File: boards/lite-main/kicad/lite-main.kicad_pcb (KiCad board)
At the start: 2 copper layers, 100 x 90 mm, 149 parts, among them J1 TYPE-C-31-M-12, J2 RCA line in, J3 RCA sub out, J4 DB128V-5.08-4P, Q1 AO4485, Q2 MMBT3904, Q3 MMBT3904, Q4 MMBT3904, SW1 TS-1187A, SW2 TS-1187A, SW3 TS-1187A, U1 CH224A, U2 TPS54302, U3 SY8089A1AAC, U4 LP5907-3.3, U5 ESP32-WROVER-E-N8R8, U6 CH340B, U7 ES8388, U8 TPA3118D2, U9 IRM-3638T

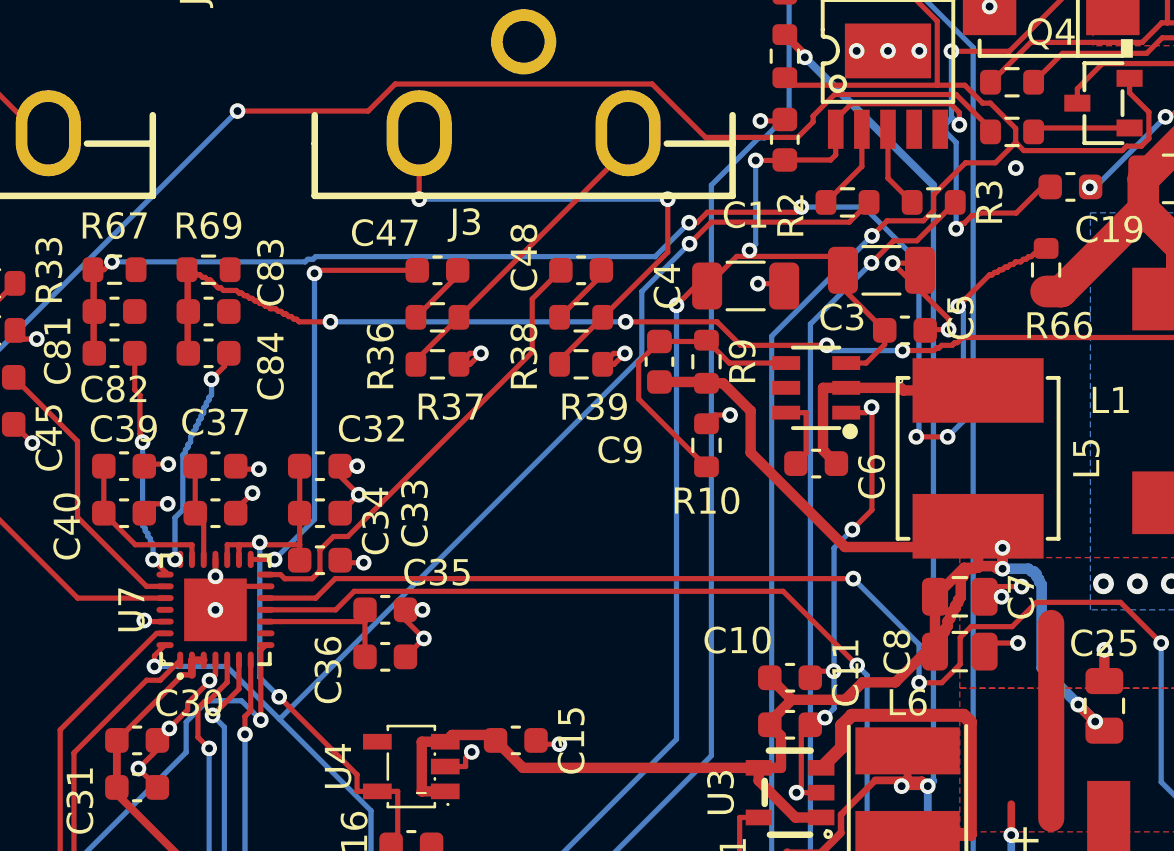
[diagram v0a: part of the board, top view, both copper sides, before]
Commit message: Lite's sub outs mute on power loss (review-3 R3-AUDIO-2): a +5V sense holds two back-to-back 2N7002s off; when +5V drops they short SUB_L/SUB_R to GND from a 22 uF reservoir for seconds
The as-built thump at a 10k sub input was -1.61 V (full scale); with the mute
it is -25 mV (docs/review-3/sims/fix/lite_mute/tb_powerloss). Off, the gates
sit at Q12's saturation, so the sub line has to stay above -Vth(min) 1.0 V:
firmware caps LOUT2/ROUT2 at -6 dB (0.71 V peak, tb_play_cap; was +4.5 dB).
Q11 is an MMBT3904 as a diode, so no new part numbers beyond the basic
2N7002 (C8545). 9 parts placed in the free pocket under R37-R39 and routed
with miniroute; two GND vias rejoin the pour the new tracks split. DRC clean
(zones refilled), drc_routed and dfm gates pass, fab files regenerated.

Also Lite's thermal governor 13 -> 9 W a channel (R3-LAYOUT-13).
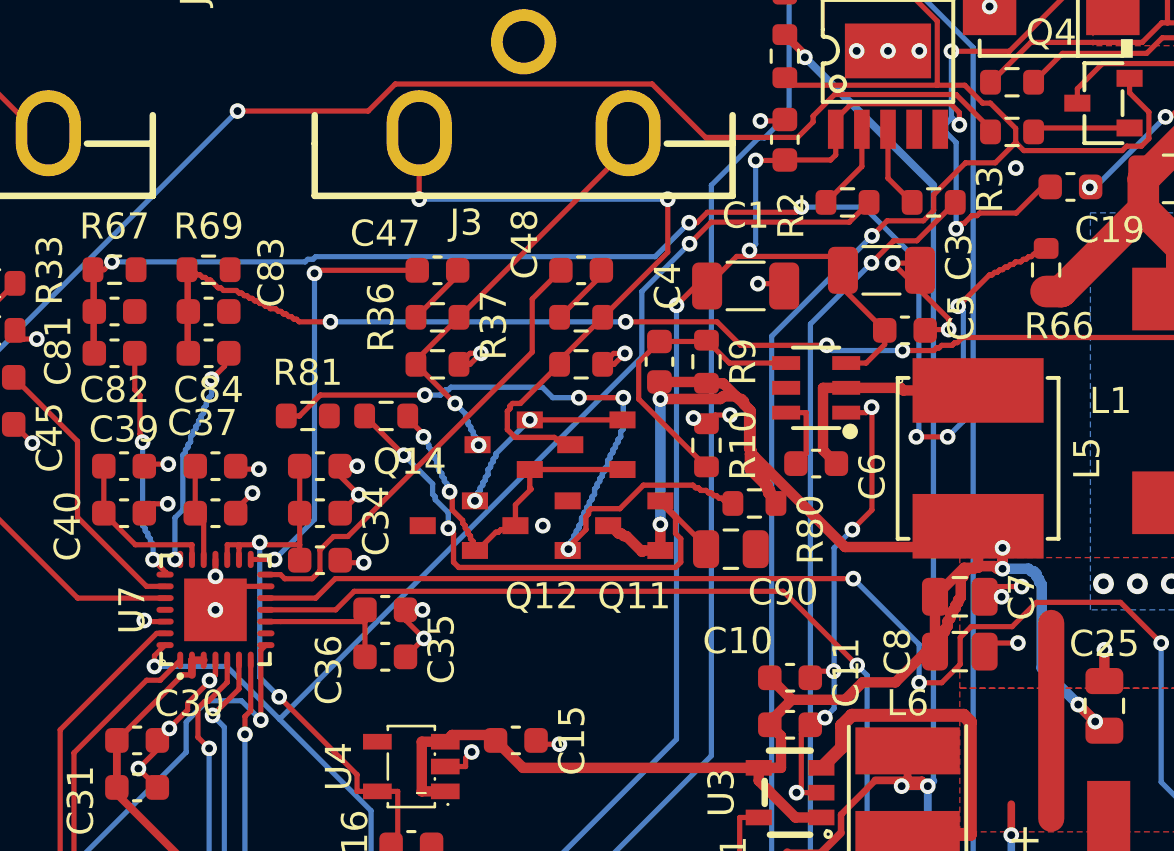
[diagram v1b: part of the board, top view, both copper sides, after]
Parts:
- added C90: 22uF, Capacitor_SMD:C_0805_2012Metric, F.Cu at (72.6, 93.0)
- added Q11: MMBT3904, aiee:SOT-23-3_L2.9-W1.3-P1.90-LS2.4-BR, F.Cu at (68.9, 92.1)
- added Q12: MMBT3904, aiee:SOT-23-3_L2.9-W1.3-P1.90-LS2.4-BR, F.Cu at (65.3, 92.1)
- added Q13: 2N7002, aiee:SOT-23-3_L2.9-W1.3-P1.90-LS2.4-BR, F.Cu at (63.9, 89.0)
- added Q14: 2N7002, aiee:SOT-23-3_L2.9-W1.3-P1.90-LS2.4-BR, F.Cu at (61.8, 92.1)
- added Q15: 2N7002, aiee:SOT-23-3_L2.9-W1.3-P1.90-LS2.4-BR, F.Cu at (67.5, 89.0)
- added R80: 120k, Resistor_SMD:R_0603_1608Metric, F.Cu at (73.5, 91.2)
- added R81: 22k, Resistor_SMD:R_0603_1608Metric, F.Cu at (56.4, 87.9)
- added R82: 47k, Resistor_SMD:R_0603_1608Metric, F.Cu at (59.4, 87.9)
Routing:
- net /MUTE_DET: track 0.00 -> 28.2 mm, vias 0 -> 4
- net /MUTE_RES: track 0.00 -> 21.1 mm, vias 0 -> 2
- net +5V: track 68.9 -> 87.2 mm, vias 4 -> 6
- net /SUB_MUTE: track 0.00 -> 14.2 mm, vias 0 -> 2
- net /MUTE_S: track 0.00 -> 7.52 mm, vias 0 -> 2
- net /SUB_R: track 21.1 -> 27.3 mm
- net /SUB_L: track 11.8 -> 15.9 mm, vias 0 -> 2
- net GND: vias 117 -> 119

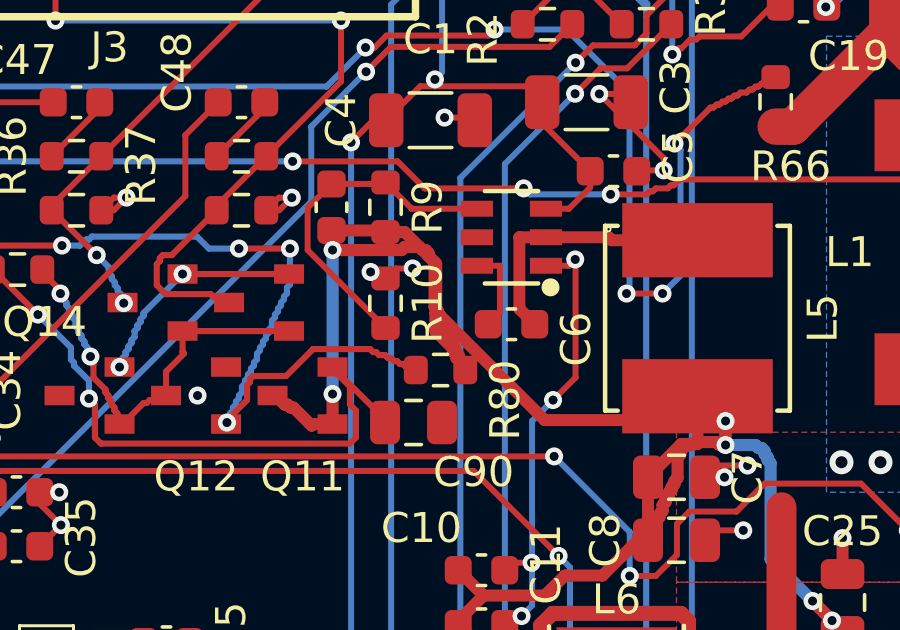
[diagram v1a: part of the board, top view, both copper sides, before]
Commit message: Lite sub build-out R36/R38 100R -> 1k (R4-PAD-1), fab regenerated
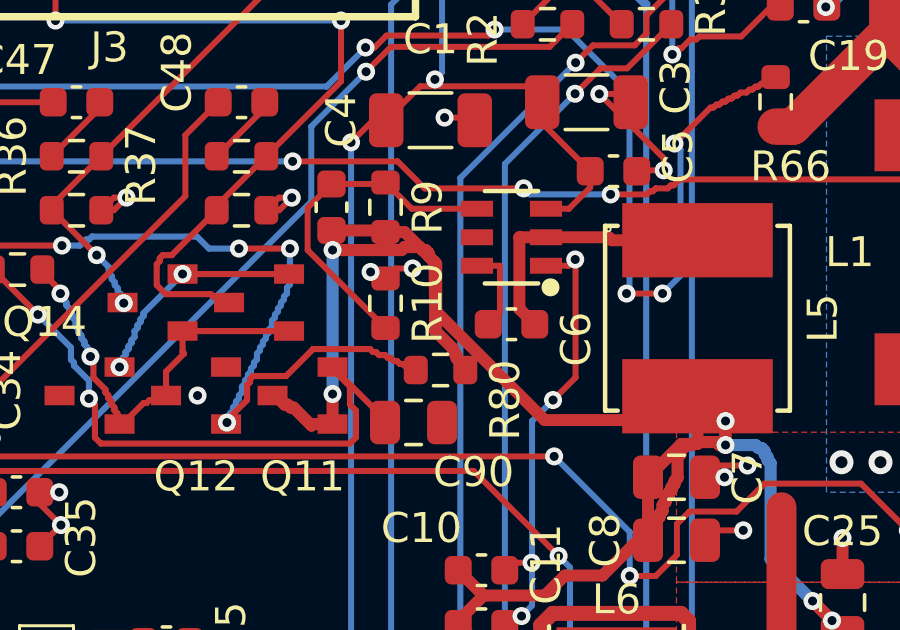
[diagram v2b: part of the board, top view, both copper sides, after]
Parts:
- R36, R38: value 100R -> 1k
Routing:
- net +5V: track 87.2 -> 85.5 mm
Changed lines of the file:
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@@
 			)
 		)
-		(property "Value" "100R"
+		(property "Value" "1k"
 			(at 0 1.43 0)
 			(layer "F.Fab")
@@
 			)
 		)
-		(property "LCSC" "C22775"
+		(property "LCSC" "C21190"
 			(at 0 0 0)
 			(layer "F.SilkS")
@@
 			)
 		)
-		(property "Value" "100R"
+		(property "Value" "1k"
 			(at 0 1.43 0)
 			(layer "F.Fab")
@@
 			)
 		)
-		(property "LCSC" "C22775"
+		(property "LCSC" "C21190"
 			(at 0 0 0)
 			(layer "F.SilkS")
@@
 	)
 	(segment
-		(start 73.1 87.35)
-		(end 73.1 87.45)
-		(width 0.405)
-		(layer "F.Cu")
-		(net "+5V")
-	)
-	(segment
 		(start 76.971 92.9173)
 		(end 73.3569 89.3032)
@@
 	)
 	(segment
-		(start 74.2 90.95)
-		(end 74.2 91.05)
-		(width 0.405)
-		(layer "F.Cu")
-		(net "+5V")
-	)
-	(segment
-		(start 74.3 91.15)
-		(end 74.33 91.18)
-		(width 0.405)
-		(layer "F.Cu")
-		(net "+5V")
-	)
-	(segment
 		(start 83 93.75)
 		(end 83 92.95)
@@
 	)
 	(segment
-		(start 74.2 91.05)
-		(end 74.3 91.15)
-		(width 0.405)
-		(layer "F.Cu")
-		(net "+5V")
-	)
-	(segment
 		(start 68.4 92.4)
 		(end 68.5 92.5)
@@
 	)
 	(segment
-		(start 74.1 90.85)
-		(end 74.2 90.95)
-		(width 0.405)
-		(layer "F.Cu")
-		(net "+5V")
-	)
-	(segment
 		(start 69.865 86.598)
 		(end 71.615 86.598)
@@
 	)
 	(segment
-		(start 72.3 87.15)
-		(end 72.8 87.15)
-		(width 0.405)
-		(layer "F.Cu")
-		(net "+5V")
-	)
-	(segment
 		(start 80.415 96.923)
 		(end 80.415 94.823)
@@
 	)
 	(segment
-		(start 73.5 89.55)
-		(end 73.6 89.65)
-		(width 0.405)
-		(layer "F.Cu")
-		(net "+5V")
-	)
-	(segment
 		(start 81 95.55)
 		(end 81 95.65)
@@
 	)
 	(segment
-		(start 72.2 87.25)
-		(end 72.3 87.15)
+		(start 73 87.25)
+		(end 73.1 87.35)
 		(width 0.405)
 		(layer "F.Cu")
@@
 	)
 	(segment
-		(start 74.1 90.75)
-		(end 74.1 90.85)
-		(width 0.405)
-		(layer "F.Cu")
-		(net "+5V")
-	)
-	(segment
 		(start 77.6421 98.0993)
 		(end 76.9747 98.7667)
@@
 	)
 	(segment
-		(start 81.2 95.25)
-		(end 81.1 95.35)
-		(width 0.405)
-		(layer "F.Cu")
-		(net "+5V")
-	)
-	(segment
-		(start 73.4 89.35)
-		(end 73.5 89.45)
+		(start 72.3 87.15)
+		(end 72.8 87.15)
 		(width 0.405)
 		(layer "F.Cu")
@@
 	)
 	(segment
-		(start 72.9 87.25)
-		(end 73 87.25)
+		(start 81.2 95.25)
+		(end 81.1 95.35)
 		(width 0.405)
 		(layer "F.Cu")
@@
 	)
 	(segment
-		(start 73.6 89.65)
-		(end 73.6 89.75)
-		(width 0.405)
-		(layer "F.Cu")
-		(net "+5V")
-	)
-	(segment
 		(start 67.9 92.1)
 		(end 68 92.2)
@@
 	)
 	(segment
-		(start 69.9 87.25)
-		(end 72.2 87.25)
-		(width 0.405)
-		(layer "F.Cu")
-		(net "+5V")
-	)
-	(segment
 		(start 81.1 95.45)
 		(end 81 95.55)
@@
 	)
 	(segment
-		(start 73 87.25)
-		(end 73.1 87.35)
+		(start 73.33 89.95)
+		(end 73.33 89.35)
 		(width 0.405)
 		(layer "F.Cu")
@@
 	)
 	(segment
-		(start 73.33 89.95)
-		(end 73.33 89.35)
+		(start 81.3 95.05)
+		(end 81.2 95.15)
 		(width 0.405)
 		(layer "F.Cu")
@@
 	)
 	(segment
-		(start 81.3 95.05)
-		(end 81.2 95.15)
+		(start 72.9 87.25)
+		(end 73 87.25)
 		(width 0.405)
 		(layer "F.Cu")
@@
 	)
 	(segment
-		(start 73.3 87.65)
-		(end 73.3 89.15)
-		(width 0.405)
+		(start 76.9747 98.7667)
+		(end 74.9337 98.7667)
+		(width 0.4)
 		(layer "F.Cu")
 		(net "+5V")
 	)
 	(segment
-		(start 76.9747 98.7667)
-		(end 74.9337 98.7667)
-		(width 0.4)
+		(start 72.8 87.15)
+		(end 72.9 87.25)
+		(width 0.405)
 		(layer "F.Cu")
 		(net "+5V")
@@
 	)
 	(segment
-		(start 74.9337 98.7667)
-		(end 74.09 99.6104)
-		(width 0.4)
+		(start 72.2 87.25)
+		(end 72.3 87.15)
+		(width 0.405)
 		(layer "F.Cu")
 		(net "+5V")
 	)
 	(segment
-		(start 73.9 90.45)
-		(end 74 90.55)
-		(width 0.405)
+		(start 74.9337 98.7667)
+		(end 74.09 99.6104)
+		(width 0.4)
 		(layer "F.Cu")
 		(net "+5V")
@@
 	)
 	(segment
-		(start 73.7 89.95)
-		(end 73.8 90.05)
-		(width 0.405)
-		(layer "F.Cu")
-		(net "+5V")
-	)
-	(segment
-		(start 74 90.55)
-		(end 74 90.65)
-		(width 0.405)
-		(layer "F.Cu")
-		(net "+5V")
-	)
-	(segment
 		(start 74.33 91.25)
 		(end 74.23 91.15)
@@
 	)
 	(segment
-		(start 69.9 93.05)
-		(end 69.9 92.05)
-		(width 0.405)
-		(layer "F.Cu")
-		(net "+5V")
-	)
-	(segment
 		(start 83 93.75)
 		(end 82.8 93.75)
@@
 	)
 	(segment
-		(start 73.8 90.05)
-		(end 73.8 90.25)
-		(width 0.405)
-		(layer "F.Cu")
-		(net "+5V")
-	)
-	(segment
 		(start 80.5 96.75)
 		(end 80.4 96.85)
@@
 	)
 	(segment
-		(start 74 90.65)
-		(end 74.1 90.75)
-		(width 0.405)
-		(layer "F.Cu")
-		(net "+5V")
-	)
-	(segment
-		(start 73.9 90.35)
-		(end 73.9 90.45)
+		(start 73.1 87.45)
+		(end 73.3 87.65)
 		(width 0.405)
 		(layer "F.Cu")
@@
 	)
 	(segment
-		(start 72.8 87.15)
-		(end 72.9 87.25)
-		(width 0.405)
-		(layer "F.Cu")
-		(net "+5V")
-	)
-	(segment
 		(start 74.09 99.6104)
 		(end 74.09 99.723)
@@
 	)
 	(segment
-		(start 73.6 89.75)
-		(end 73.7 89.85)
-		(width 0.405)
-		(layer "F.Cu")
-		(net "+5V")
-	)
-	(segment
-		(start 73.4 89.25)
-		(end 73.4 89.35)
+		(start 69.9 93.05)
+		(end 69.9 92.05)
 		(width 0.405)
 		(layer "F.Cu")
@@
 	)
 	(segment
-		(start 73.8 90.25)
-		(end 73.9 90.35)
-		(width 0.405)
+		(start 82.065 92.9173)
+		(end 82.065 93.7117)
+		(width 0.4)
 		(layer "F.Cu")
 		(net "+5V")
 	)
 	(segment
-		(start 82.065 92.9173)
-		(end 82.065 93.7117)
-		(width 0.4)
+		(start 69.9 87.25)
+		(end 72.2 87.25)
+		(width 0.405)
 		(layer "F.Cu")
 		(net "+5V")
@@
 	)
 	(segment
-		(start 73.3 89.15)
-		(end 73.4 89.25)
-		(width 0.405)
-		(layer "F.Cu")
-		(net "+5V")
-	)
-	(segment
 		(start 80.9 95.95)
 		(end 80.8 96.05)
@@
 	)
 	(segment
-		(start 73.7 89.85)
-		(end 73.7 89.95)
+		(start 80.9 95.75)
+		(end 80.9 95.95)
 		(width 0.405)
 		(layer "F.Cu")
@@
 	)
 	(segment
-		(start 80.9 95.75)
-		(end 80.9 95.95)
+		(start 74.23 91.05)
+		(end 74.03 90.85)
 		(width 0.405)
 		(layer "F.Cu")
@@
 	)
 	(segment
-		(start 74.23 91.05)
-		(end 74.03 90.85)
+		(start 73.3 87.65)
+		(end 73.33 89.95)
 		(width 0.405)
 		(layer "F.Cu")
@@
 	)
 	(segment
-		(start 73.1 87.45)
-		(end 73.3 87.65)
+		(start 73.1 87.35)
+		(end 73.1 87.45)
 		(width 0.405)
 		(layer "F.Cu")
@@
 	)
 	(segment
-		(start 73.5 89.45)
-		(end 73.5 89.55)
-		(width 0.405)
-		(layer "F.Cu")
-		(net "+5V")
-	)
-	(segment
 		(start 82.065 93.7117)
 		(end 81.5263 93.7117)
@@
 	)
 	(via
-		(at 85.9 98.95)
+		(at 69.9 92.05)
 		(size 0.6)
 		(drill 0.3)
@@
 	)
 	(via
-		(at 69.9 92.05)
+		(at 85.9 98.95)
 		(size 0.6)
 		(drill 0.3)
@@
 	)
 	(segment
+		(start 69.9 92.05)
+		(end 69.9 87.25)
+		(width 0.405)
+		(layer "B.Cu")
+		(net "+5V")
+	)
+	(segment
 		(start 84.1 93.85)
 		(end 84 93.75)
@@
 		(width 0.405)
 		(layer "B.Cu")
-		(net "+5V")
-	)
-	(segment
-		(start 69.9 92.05)
-		(end 69.9 87.25)
-		(width 0.405)
-		(layer "B.Cu")
